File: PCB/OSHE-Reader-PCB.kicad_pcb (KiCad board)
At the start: 2 copper layers, 100 x 100 mm, 66 parts, among them Q1 Si1308EDL, Q2 BSS138, Q3 BSS138, U1 74LVC1G04, U2 TPS923610DRLR, U3 TLV75533PDBV

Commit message: Changed the Thermistor
OMG WE FINALLY FIXED THE THERMISTOR FOOTPRINT
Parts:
- TH1: footprint Connector_JST:JST_EH_B11B-EH-A_1x11_P2.50mm_Vertical -> Connector_PinHeader_2.00mm:PinHeader_1x02_P2.00mm_Vertical
- moved R3 19.1 mm to (178.5, 125.0), turned to -90 degrees
- moved R4 16.5 mm to (178.5, 113.5), turned to 90 degrees
- moved TH1 13.0 mm to (122.0, 55.5), turned to 180 degrees
- moved bottom_right_button1 10.3 mm to (188.8, 126.5)
- moved top_right_button1 10.3 mm to (188.5, 111.5)
- moved R5 9.89 mm to (126.3, 113.0)
- moved R6 9.89 mm to (126.3, 124.5)
- moved bottom_left_button1 9.89 mm to (117.8, 126.0)
- moved top_left_button1 9.89 mm to (117.8, 111.5)
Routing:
- net /BR_button: track 105.8 -> 0.00 mm, vias 2 -> 0
- net /TR_button: track 88.3 -> 0.00 mm, vias 2 -> 0
- net /BL_button: track 84.7 -> 0.40 mm
- net /STAT: track 79.9 -> 0.00 mm, vias 2 -> 0
- net /TL_button: track 73.2 -> 0.30 mm
- net GND: track 72.4 -> 0.99 mm
- net /3V3: track 18.0 -> 0.00 mm
- net unconnected-(display_connector1-MountPin-PadMP): track 15.3 -> 0.00 mm
- net /BAT+: track 13.1 -> 0.85 mm
- net /Battery Charger/SW: track 7.93 -> 0.50 mm
- net unconnected-(to_battery1-MountPin-PadMP): track 6.70 -> 0.00 mm
- net /VBUS: track 7.62 -> 1.36 mm
- net /Battery Charger/SYS: track 6.55 -> 0.50 mm
- net Net-(D8-K): track 6.05 -> 0.18 mm
- net /HOME_button: track 5.50 -> 0.00 mm
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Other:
- board size 100 x 100 mm -> 80 x 100 mm

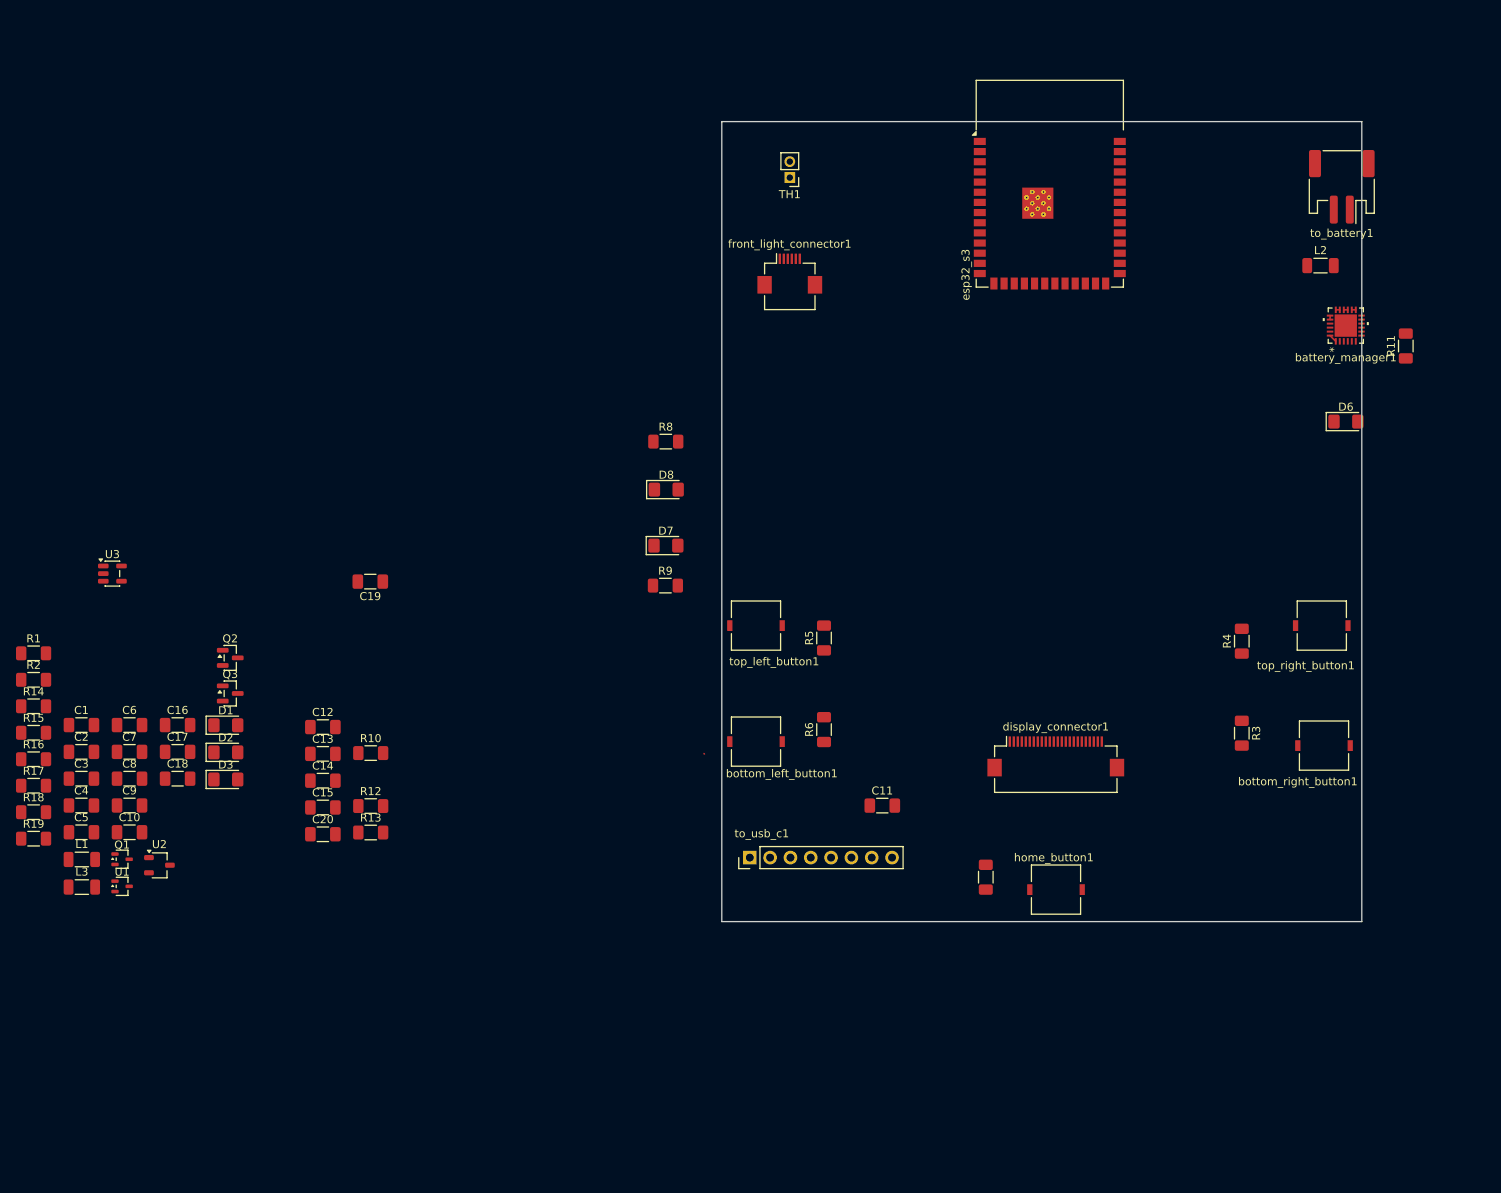
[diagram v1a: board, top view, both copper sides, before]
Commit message: Rechecked schematic + started PCB
Schematic:
+ routed screen connector
+ fixed charger to 500mA and routed data to MCU
+ added micro sd card reader
+ added uart, jtag, and boot selector pins
= changed esp32 symbol
= made 3v3 a power symbol (idk why i didnt do this from the start)

TODO:
pick resistor values for thermistor
put all passives on pcb
route pcb
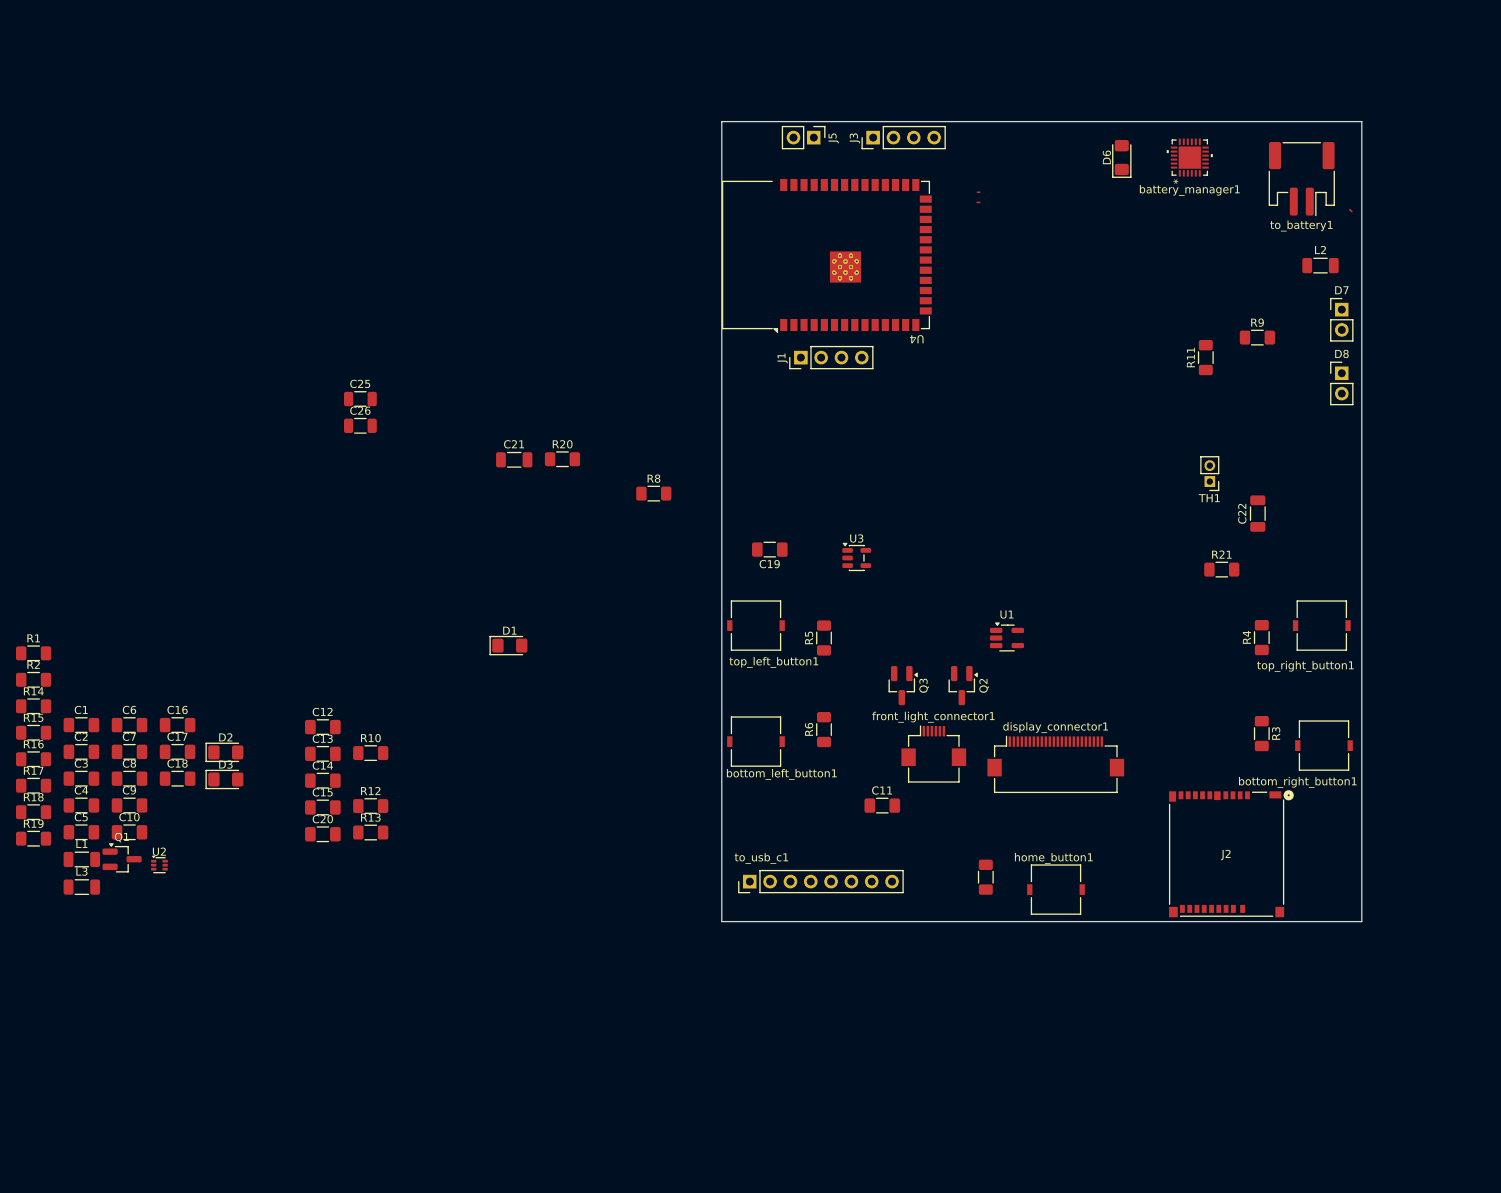
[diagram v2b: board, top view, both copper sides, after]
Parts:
- removed esp32_s3: ESP32-S3-WROOM-1-N8R8, RF_Module:ESP32-S3-WROOM-1
- added C21: 1uF, Inductor_SMD:L_1206_3216Metric_Pad1.22x1.90mm_HandSolder, F.Cu at (87.6, 90.8)
- added C22: 1uF, Inductor_SMD:L_1206_3216Metric_Pad1.22x1.90mm_HandSolder, F.Cu at (180.5, 97.5)
- added C25: 0.1uF, Capacitor_SMD:C_1206_3216Metric, F.Cu at (68.3, 83.2)
- added C26: 10uF, Capacitor_SMD:C_1206_3216Metric, F.Cu at (68.3, 86.5)
- added J1: UART, Connector_PinHeader_2.54mm:PinHeader_1x04_P2.54mm_Vertical, F.Cu at (123.4, 78.0)
- added J2: 112L-TDA0, 112L-TDA0:CONN_112L-TDA0_ATT, F.Cu at (176.6, 140.1)
- added J3: JTAG, Connector_PinHeader_2.54mm:PinHeader_1x04_P2.54mm_Vertical, F.Cu at (132.4, 50.5)
- added J5: boot_select, Connector_PinHeader_2.54mm:PinHeader_1x02_P2.54mm_Vertical, F.Cu at (125.0, 50.5)
- added R20: 10k, Resistor_SMD:R_1206_3216Metric_Pad1.30x1.75mm_HandSolder, F.Cu at (93.6, 90.7)
- added R21: 10k, Resistor_SMD:R_1206_3216Metric_Pad1.30x1.75mm_HandSolder, F.Cu at (176.0, 104.5)
- added U4: ESP32-S3-WROOM-1, RF_Module:ESP32-S3-WROOM-1, F.Cu at (126.5, 65.2)
- D7, D8: footprint LED_SMD:LED_1206_3216Metric_Pad1.42x1.75mm_HandSolder -> Connector_PinHeader_2.54mm:PinHeader_1x02_P2.54mm_Vertical
- Q1: footprint Package_TO_SOT_SMD:SOT-323_SC-70 -> Package_TO_SOT_SMD:SOT-23_Handsoldering
- Q2, Q3: footprint Package_TO_SOT_SMD:SOT-23 -> Package_TO_SOT_SMD:SOT-23_Handsoldering
- R10: value R -> 1.5k
- R11: value R -> 1k
- R8, R9: value R -> 10k
- U1: footprint Package_TO_SOT_SMD:SOT-323_SC-70 -> Package_TO_SOT_SMD:SOT-23-5_HandSoldering
- U2: footprint Package_TO_SOT_SMD:TSOT-23 -> Package_TO_SOT_SMD:SOT-563
- moved U1 114.9 mm to (149.2, 113.0)
- moved U3 93.1 mm to (130.4, 103.0)
- moved Q2 91.5 mm to (143.5, 119.0), turned to -90 degrees
- moved D7 89.5 mm to (191.0, 72.0)
- moved D8 85.7 mm to (191.0, 80.0)
- moved Q3 84.0 mm to (136.0, 119.0), turned to -90 degrees
- moved R9 80.2 mm to (180.4, 75.5)
- moved TH1 64.8 mm to (174.5, 93.5)
- moved front_light_connector1 61.7 mm to (140.0, 126.5)
- moved C19 50.1 mm to (119.5, 102.0)
- moved D6 43.3 mm to (163.5, 53.0), turned to 90 degrees
- moved D1 36.9 mm to (87.0, 114.0)
- moved battery_manager1 28.7 mm to (172.0, 53.0)
- moved R11 25.0 mm to (174.0, 78.0)
- moved R8 6.67 mm to (105.0, 95.0)
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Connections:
- C16 pad 1: /3V3 -> +3V3
- C19 pad 1: /3V3 -> +3V3
- C9 pad 1: /3V3 -> +3V3
- L1 pad 1: /3V3 -> +3V3
- R3 pad 1: /3V3 -> +3V3
- R4 pad 1: /3V3 -> +3V3
- R5 pad 1: /3V3 -> +3V3
- R6 pad 1: /3V3 -> +3V3
- R7 pad 1: /3V3 -> +3V3
- U3 pad 5: /3V3 -> +3V3
- battery_manager1 pad 3: /D+ -> unconnected-(battery_manager1-D+-Pad3)
- battery_manager1 pad 4: /D- -> unconnected-(battery_manager1-D--Pad4)
- display_connector1 pad 10: /Display + Front Light/RES# -> /RES_SCR
- display_connector1 pad 11: /Display + Front Light/D/C# -> /D/C
- display_connector1 pad 12: /Display + Front Light/CS# -> /EPAP_CS
- display_connector1 pad 13: /Display + Front Light/SCL -> /SCL
- display_connector1 pad 14: /Display + Front Light/SDA -> /COPI
- display_connector1 pad 19: /Display + Front Light/VPP -> unconnected-(display_connector1-Pin_19-Pad19)
- display_connector1 pad 9: /Display + Front Light/BUSY -> /BUSY
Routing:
- net /VBUS: track 1.36 -> 0.00 mm
- net GND: track 0.99 -> 0.00 mm
- net /Battery Charger/SYS: track 0.50 -> 0.00 mm
- net /Battery Charger/SW: track 0.50 -> 0.00 mm
- net /BAT+: track 0.85 -> 0.35 mm

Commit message: PCB Routing
-Added Ryan's numbers for the battery manager resistors and stuff.
-Started routing the PCB and laying out some resistors and caps off to the side to make nice easy routing chains.
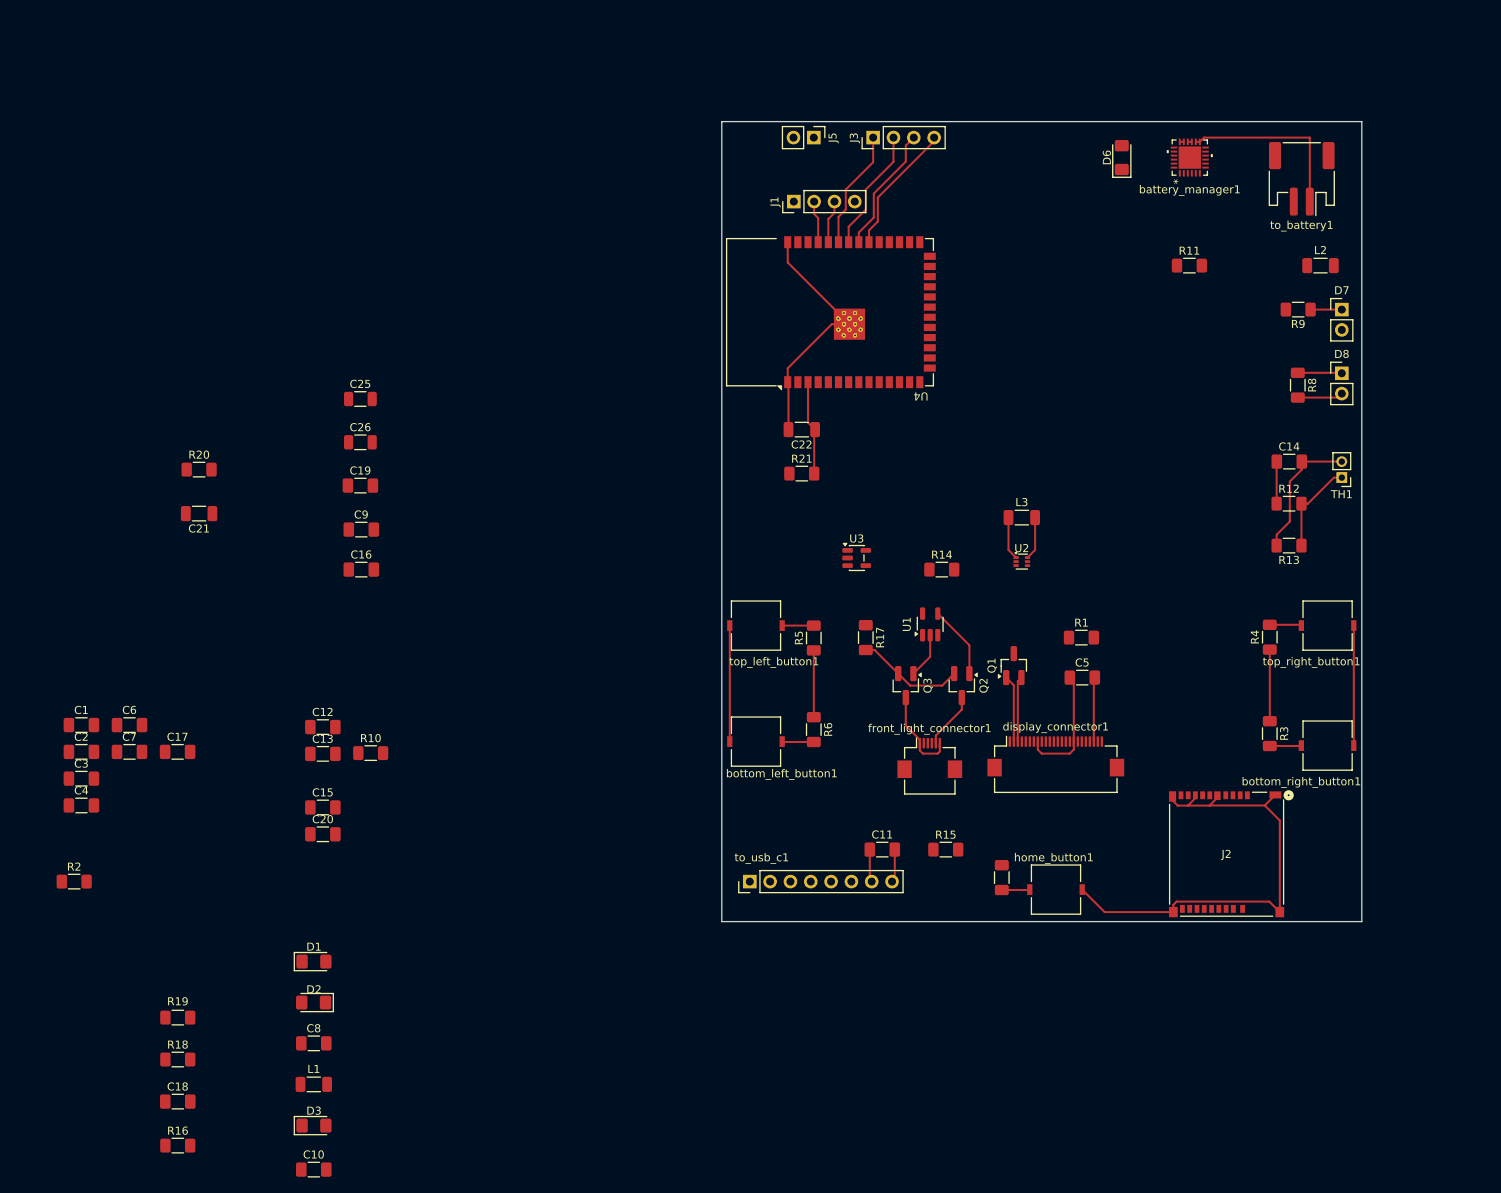
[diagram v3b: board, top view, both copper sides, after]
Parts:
- R10: value 1.5k -> 953
- R11: value 1k -> 2.26k
- R12: value R -> 5.3k
- R13: value R -> 31.14k
- R8, R9: value 10k -> 680
- TH1: value Thermistor -> 10k
- moved R1 131.0 mm to (158.4, 113.0)
- moved C14 127.2 mm to (184.4, 91.0)
- moved C5 126.6 mm to (158.6, 118.0)
- moved L3 126.2 mm to (151.0, 98.0)
- moved R12 120.9 mm to (184.4, 96.3)
- moved R13 120.3 mm to (184.4, 101.5), turned to 180 degrees
- moved R15 115.0 mm to (141.5, 139.5)
- moved R14 114.8 mm to (141.0, 104.5)
- moved U2 114.3 mm to (151.0, 103.5)
- moved Q1 114.1 mm to (150.0, 116.5), turned to 90 degrees
- moved R17 105.7 mm to (131.5, 113.0), turned to -90 degrees
- moved R8 81.6 mm to (185.5, 81.5), turned to -90 degrees
- moved C22 58.0 mm to (123.5, 87.0), turned to 180 degrees
- moved R21 53.9 mm to (123.5, 92.5)
- moved C19 51.8 mm to (68.3, 94.0), turned to 0 degrees
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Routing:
- net GND: track 0.00 -> 156.3 mm
- net /BAT+: track 0.35 -> 22.5 mm
- net +3V3: track 0.00 -> 17.3 mm
- net /TCK: track 0.00 -> 16.4 mm
- net /TDO: track 0.00 -> 15.9 mm
- net /TDI: track 0.00 -> 15.4 mm
- net /TMS: track 0.00 -> 14.9 mm
- net Net-(Q2-S): track 0.00 -> 13.5 mm
- net Net-(U4-EN): track 0.00 -> 11.8 mm
- net /Battery Charger/TS: track 0.00 -> 11.6 mm
- net /Display + Front Light/LED_C+: track 0.00 -> 11.1 mm
- net /Display + Front Light/COLOR_SEL_INV: track 0.00 -> 9.14 mm
- net /Display + Front Light/GDR: track 0.00 -> 8.39 mm
- net /Display + Front Light/RESE: track 0.00 -> 8.19 mm
- net /Display + Front Light/VSL: track 0.00 -> 8.05 mm
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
